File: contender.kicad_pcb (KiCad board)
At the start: 2 copper layers, 105.3 x 130.9 mm, 142 parts, among them SW1 SW_Push, U1 ATmega32U2-AU, U2 PRTR5V0U2X, Y1 16MHz

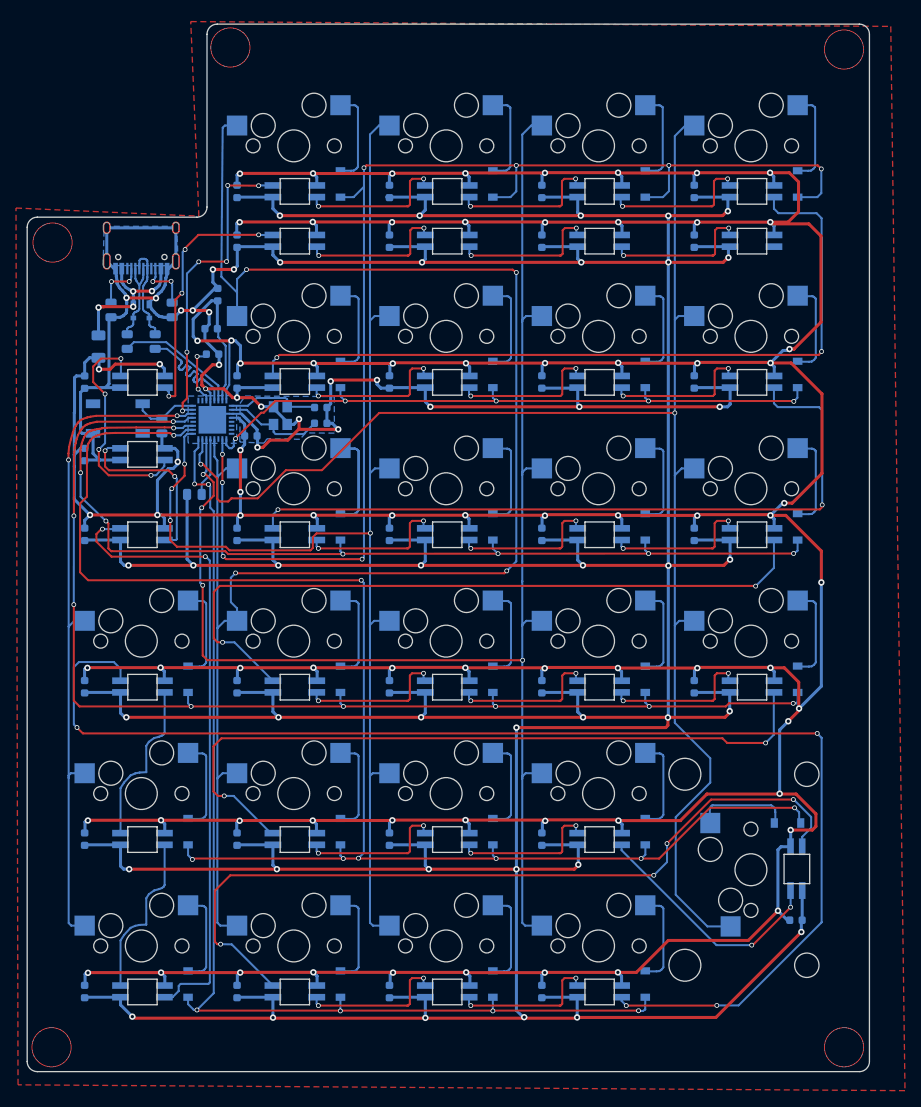
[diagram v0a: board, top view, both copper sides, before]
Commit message: fix led footpring & v1.1 commit
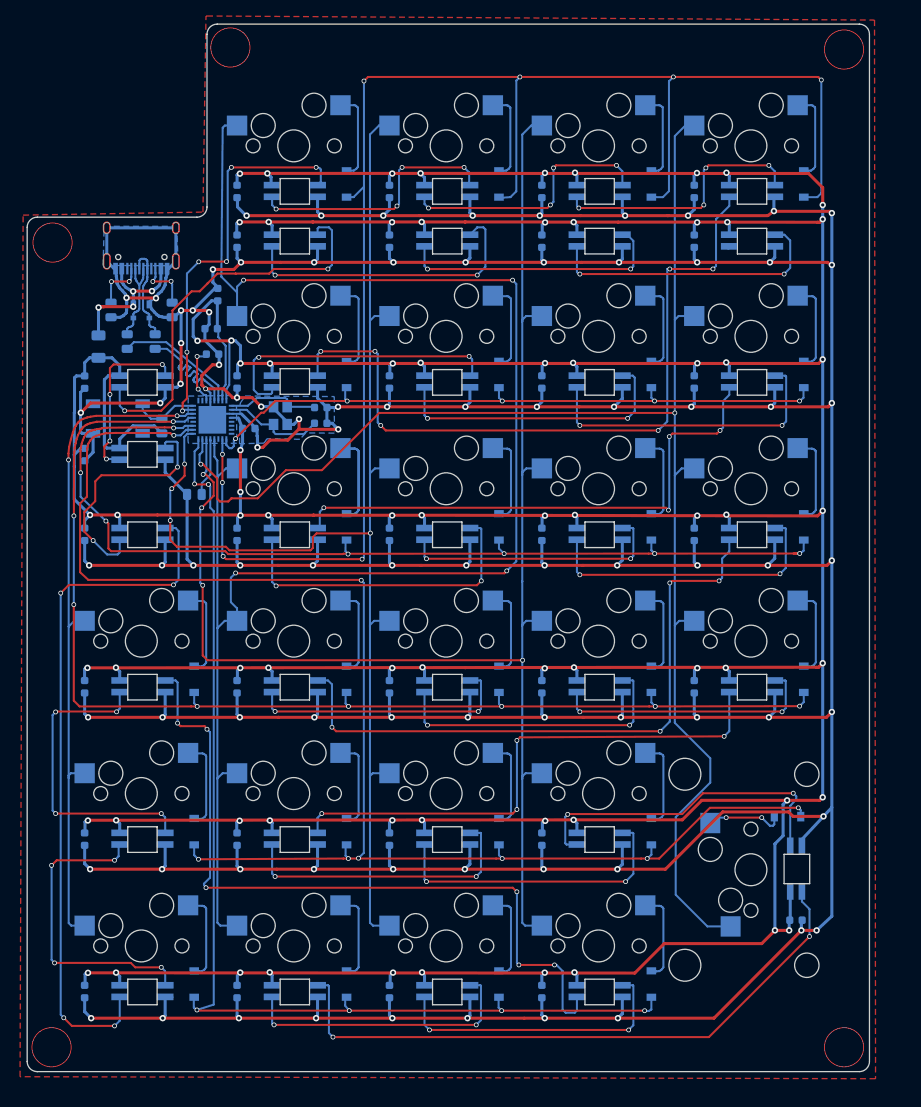
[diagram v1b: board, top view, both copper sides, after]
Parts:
- L1, L10, L11, L12, L13, L14, L15, L16, L17, L18, L19, L2, L20, L21, L22, L23, L24, L25, L26, L27, L28, L29, L3, L30, L31, L32, L33, L4, L5, L6, L7, L8, L9: footprint sk6812mini-e:YS-SK6812_backlight -> sk6812mini-e:YS-SK6812-MINI-E_backlight
- moved C3 0.97 mm to (50.3, 70.1)
- moved D20 0.80 mm to (117.7, 118.6)
- moved D1 0.76 mm to (62.5, 39.5)
- moved D10 0.76 mm to (81.6, 82.4)
- moved D11 0.76 mm to (100.6, 82.4)
- moved D12 0.76 mm to (119.7, 82.4)
- moved D13 0.76 mm to (62.5, 101.4)
- moved D14 0.76 mm to (81.6, 101.4)
- moved D15 0.76 mm to (100.6, 101.4)
- moved D16 0.76 mm to (119.7, 101.4)
- moved D17 0.76 mm to (62.5, 120.5)
- moved D18 0.76 mm to (81.6, 120.5)
- moved D19 0.76 mm to (100.6, 120.5)
- moved D2 0.76 mm to (81.6, 39.5)
- moved D21 0.76 mm to (62.5, 139.5)
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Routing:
- net GND: track 946.6 -> 1015.9 mm, vias 54 -> 85
- net Net-(L23-Pad2): track 162.4 -> 93.7 mm, vias 4 -> 6
- net ROWFN: track 161.3 -> 202.9 mm
- net Net-(L16-Pad2): track 91.7 -> 67.8 mm, vias 2 -> 4
- net Net-(L8-Pad2): track 91.2 -> 67.8 mm, vias 2 -> 4
- net Net-(L20-Pad2): track 101.6 -> 78.8 mm, vias 4 -> 2
- net Net-(L10-Pad4): track 18.4 -> 39.9 mm
- net Net-(L7-Pad2): track 18.4 -> 38.1 mm
- net Net-(L30-Pad2): track 18.4 -> 37.9 mm
- net Net-(L18-Pad2): track 18.4 -> 37.5 mm
- net Net-(L5-Pad2): track 18.4 -> 37.2 mm
- net Net-(L11-Pad2): track 18.4 -> 37.0 mm
- net Net-(L14-Pad2): track 18.4 -> 36.7 mm
- net Net-(L24-Pad2): track 20.9 -> 39.1 mm, vias 0 -> 4
- net Net-(L17-Pad2): track 18.4 -> 36.3 mm
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
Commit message: production release
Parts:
- U1: value ATmega32U2-AU -> ATmega32U2-MU
